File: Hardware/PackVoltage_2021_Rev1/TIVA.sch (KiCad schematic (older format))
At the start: 1 part, among them U1 TM4C129E_Launchpad

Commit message: Fixed Hierarchial Pins/Labels
Removed Hierarchal labels from top sheet and replaced them with pins linked to the subsheets.
Renamed M5 Tiva pin to D1
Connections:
- net labels added: Current_Sensor_D1, Driver_D1
- net labels removed: Current_Sensor_M5, Driver_M5
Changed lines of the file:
@@
 Wire Wire Line
 	6050 1900 6150 1900
-Text HLabel 6150 1700 2    50   Input ~ 0
-Current_Sensor_M5
-Text HLabel 6150 1900 2    50   Output ~ 0
-Driver_M5
 Wire Wire Line
 	6050 1800 6150 1800
@@
 Driver_A1
 NoConn ~ 1500 3800
+Text HLabel 6150 1900 2    50   Output ~ 0
+Driver_D1
+Text HLabel 6150 1700 2    50   Input ~ 0
+Current_Sensor_D1
 $EndSCHEMATC

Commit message: added extra 12V pin to TIVA
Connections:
- net labels added: ExtraCTL
- wire segments 43 -> 44
- no-connect marks 45 -> 44
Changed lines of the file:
@@
 NoConn ~ 1500 4000
 NoConn ~ 1500 4100
-NoConn ~ 1500 4400
 NoConn ~ 2500 4200
 Text HLabel 1350 1200 1    50   Input ~ 0
@@
 Text HLabel 6150 1700 2    50   Input ~ 0
 Current_Sensor_D1
+Text HLabel 1400 4400 0    50   Output ~ 0
+ExtraCTL
+Wire Wire Line
+	1500 4400 1400 4400
 $EndSCHEMATC

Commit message: Added GimbalSense, reannotated
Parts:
- renumbered U1 to U24
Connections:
- net labels added: GimbalSense
- wire segments 44 -> 45
- no-connect marks 44 -> 43
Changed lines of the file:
@@
 $EndDescr
 $Comp
-L MRDT_Shields:TM4C129E_Launchpad U1
+L MRDT_Shields:TM4C129E_Launchpad U24
 U 2 1 5F7739FC
 P 2300 2150
-F 0 "U1" H 2331 3427 60  0000 C CNN
+F 0 "U24" H 2331 3427 60  0000 C CNN
 F 1 "TM4C129E_Launchpad" H 2331 3321 60  0000 C CNN
 F 2 "" H 2300 2150 60  0001 C CNN
@@
 $EndComp
 $Comp
-L MRDT_Shields:TM4C129E_Launchpad U1
+L MRDT_Shields:TM4C129E_Launchpad U24
 U 1 1 5F776678
 P 1700 2150
-F 0 "U1" H 1650 2000 60  0000 L CNN
+F 0 "U24" H 1650 2000 60  0000 L CNN
 F 1 "TM4C129E_Launchpad" H 1300 1850 60  0000 L CNN
 F 2 "" H 1700 2150 60  0001 C CNN
@@
 	2750 2000 2500 2000
 $Comp
-L MRDT_Shields:TM4C129E_Launchpad U1
+L MRDT_Shields:TM4C129E_Launchpad U24
 U 3 1 5F782FEC
 P 5200 2150
-F 0 "U1" H 5100 1950 60  0000 L CNN
+F 0 "U24" H 5100 1950 60  0000 L CNN
 F 1 "TM4C129E_Launchpad" H 4700 1800 60  0000 L CNN
 F 2 "" H 5200 2150 60  0001 C CNN
@@
 $EndComp
 $Comp
-L MRDT_Shields:TM4C129E_Launchpad U1
+L MRDT_Shields:TM4C129E_Launchpad U24
 U 4 1 5F7858A1
 P 5850 2150
-F 0 "U1" H 5881 3427 60  0000 C CNN
+F 0 "U24" H 5881 3427 60  0000 C CNN
 F 1 "TM4C129E_Launchpad" H 5881 3321 60  0000 C CNN
 F 2 "" H 5850 2150 60  0001 C CNN
@@
 $EndComp
 $Comp
-L MRDT_Shields:TM4C129E_Launchpad U1
+L MRDT_Shields:TM4C129E_Launchpad U24
 U 5 1 5F78B804
 P 1700 4550
-F 0 "U1" H 1700 4450 60  0000 L CNN
+F 0 "U24" H 1700 4450 60  0000 L CNN
 F 1 "TM4C129E_Launchpad" H 1200 4300 60  0000 L CNN
 F 2 "" H 1700 4550 60  0001 C CNN
@@
 $EndComp
 $Comp
-L MRDT_Shields:TM4C129E_Launchpad U1
+L MRDT_Shields:TM4C129E_Launchpad U24
 U 6 1 5F78DDF8
 P 2300 4550
-F 0 "U1" H 2331 5827 60  0000 C CNN
+F 0 "U24" H 2331 5827 60  0000 C CNN
 F 1 "TM4C129E_Launchpad" H 2331 5721 60  0000 C CNN
 F 2 "" H 2300 4550 60  0001 C CNN
@@
 $EndComp
 $Comp
-L MRDT_Shields:TM4C129E_Launchpad U1
+L MRDT_Shields:TM4C129E_Launchpad U24
 U 7 1 5F78FF89
 P 5050 4450
-F 0 "U1" H 4950 4300 60  0000 L CNN
+F 0 "U24" H 4950 4300 60  0000 L CNN
 F 1 "TM4C129E_Launchpad" H 4550 4200 60  0000 L CNN
 F 2 "" H 5050 4450 60  0001 C CNN
@@
 $EndComp
 $Comp
-L MRDT_Shields:TM4C129E_Launchpad U1
+L MRDT_Shields:TM4C129E_Launchpad U24
 U 8 1 5F79167F
 P 5750 4450
-F 0 "U1" H 5781 5727 60  0000 C CNN
+F 0 "U24" H 5781 5727 60  0000 C CNN
 F 1 "TM4C129E_Launchpad" H 5781 5621 60  0000 C CNN
 F 2 "" H 5750 4450 60  0001 C CNN
@@
 $EndComp
 $Comp
-L power:GND #PWR015
+L power:GND #PWR063
 U 1 1 5F7A24D9
 P 2800 1150
-F 0 "#PWR015" H 2800 900 50  0001 C CNN
+F 0 "#PWR063" H 2800 900 50  0001 C CNN
 F 1 "GND" H 2805 977 50  0000 C CNN
 F 2 "" H 2800 1150 50  0001 C CNN
@@
 	2650 1150 2800 1150
 $Comp
-L power:GND #PWR048
+L power:GND #PWR064
 U 1 1 5F7A423F
 P 2800 3550
-F 0 "#PWR048" H 2800 3300 50  0001 C CNN
+F 0 "#PWR064" H 2800 3300 50  0001 C CNN
 F 1 "GND" H 2805 3377 50  0000 C CNN
 F 2 "" H 2800 3550 50  0001 C CNN
@@
 	2650 3550 2800 3550
 $Comp
-L power:GND #PWR049
+L power:GND #PWR065
 U 1 1 5F7A4B62
 P 6250 3350
-F 0 "#PWR049" H 6250 3100 50  0001 C CNN
+F 0 "#PWR065" H 6250 3100 50  0001 C CNN
 F 1 "GND" H 6255 3177 50  0000 C CNN
 F 2 "" H 6250 3350 50  0001 C CNN
@@
 	6100 3350 6250 3350
 $Comp
-L power:GND #PWR062
+L power:GND #PWR066
 U 1 1 5F7A5110
 P 6350 1050
-F 0 "#PWR062" H 6350 800 50  0001 C CNN
+F 0 "#PWR066" H 6350 800 50  0001 C CNN
 F 1 "GND" H 6355 877 50  0000 C CNN
 F 2 "" H 6350 1050 50  0001 C CNN
@@
 NoConn ~ 2500 3600
 NoConn ~ 2500 4300
-NoConn ~ 1500 3700
 NoConn ~ 1500 3900
 NoConn ~ 4850 3500
@@
 Wire Wire Line
 	1500 4400 1400 4400
+Text HLabel 1400 3700 0    50   Input ~ 0
+GimbalSense
+Wire Wire Line
+	1400 3700 1500 3700
 $EndSCHEMATC

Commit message: updated footprints
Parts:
- U24: footprint (none) -> MRDT_Shields:TM4C129E_Launchpad_FULL_SMD_TOP; symbol MRDT_Shields:TM4C129E_Launchpad -> PackVoltage_2021_Rev1-rescue:TM4C129E_Launchpad-MRDT_Shields
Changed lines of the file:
@@
 $EndDescr
 $Comp
-L MRDT_Shields:TM4C129E_Launchpad U24
+L PackVoltage_2021_Rev1-rescue:TM4C129E_Launchpad-MRDT_Shields U24
 U 2 1 5F7739FC
 P 2300 2150
 F 0 "U24" H 2331 3427 60  0000 C CNN
 F 1 "TM4C129E_Launchpad" H 2331 3321 60  0000 C CNN
-F 2 "" H 2300 2150 60  0001 C CNN
+F 2 "MRDT_Shields:TM4C129E_Launchpad_FULL_SMD_TOP" H 2300 2150 60  0001 C CNN
 F 3 "" H 2300 2150 60  0001 C CNN
 	2    2300 2150
@@
 $EndComp
 $Comp
-L MRDT_Shields:TM4C129E_Launchpad U24
+L PackVoltage_2021_Rev1-rescue:TM4C129E_Launchpad-MRDT_Shields U24
 U 1 1 5F776678
 P 1700 2150
 F 0 "U24" H 1650 2000 60  0000 L CNN
 F 1 "TM4C129E_Launchpad" H 1300 1850 60  0000 L CNN
-F 2 "" H 1700 2150 60  0001 C CNN
+F 2 "MRDT_Shields:TM4C129E_Launchpad_FULL_SMD_TOP" H 1700 2150 60  0001 C CNN
 F 3 "" H 1700 2150 60  0001 C CNN
 	1    1700 2150
@@
 	2750 2000 2500 2000
 $Comp
-L MRDT_Shields:TM4C129E_Launchpad U24
+L PackVoltage_2021_Rev1-rescue:TM4C129E_Launchpad-MRDT_Shields U24
 U 3 1 5F782FEC
 P 5200 2150
 F 0 "U24" H 5100 1950 60  0000 L CNN
 F 1 "TM4C129E_Launchpad" H 4700 1800 60  0000 L CNN
-F 2 "" H 5200 2150 60  0001 C CNN
+F 2 "MRDT_Shields:TM4C129E_Launchpad_FULL_SMD_TOP" H 5200 2150 60  0001 C CNN
 F 3 "" H 5200 2150 60  0001 C CNN
 	3    5200 2150
@@
 $EndComp
 $Comp
-L MRDT_Shields:TM4C129E_Launchpad U24
+L PackVoltage_2021_Rev1-rescue:TM4C129E_Launchpad-MRDT_Shields U24
 U 4 1 5F7858A1
 P 5850 2150
 F 0 "U24" H 5881 3427 60  0000 C CNN
 F 1 "TM4C129E_Launchpad" H 5881 3321 60  0000 C CNN
-F 2 "" H 5850 2150 60  0001 C CNN
+F 2 "MRDT_Shields:TM4C129E_Launchpad_FULL_SMD_TOP" H 5850 2150 60  0001 C CNN
 F 3 "" H 5850 2150 60  0001 C CNN
 	4    5850 2150
@@
 $EndComp
 $Comp
-L MRDT_Shields:TM4C129E_Launchpad U24
+L PackVoltage_2021_Rev1-rescue:TM4C129E_Launchpad-MRDT_Shields U24
 U 5 1 5F78B804
 P 1700 4550
 F 0 "U24" H 1700 4450 60  0000 L CNN
 F 1 "TM4C129E_Launchpad" H 1200 4300 60  0000 L CNN
-F 2 "" H 1700 4550 60  0001 C CNN
+F 2 "MRDT_Shields:TM4C129E_Launchpad_FULL_SMD_TOP" H 1700 4550 60  0001 C CNN
 F 3 "" H 1700 4550 60  0001 C CNN
 	5    1700 4550
@@
 $EndComp
 $Comp
-L MRDT_Shields:TM4C129E_Launchpad U24
+L PackVoltage_2021_Rev1-rescue:TM4C129E_Launchpad-MRDT_Shields U24
 U 6 1 5F78DDF8
 P 2300 4550
 F 0 "U24" H 2331 5827 60  0000 C CNN
 F 1 "TM4C129E_Launchpad" H 2331 5721 60  0000 C CNN
-F 2 "" H 2300 4550 60  0001 C CNN
+F 2 "MRDT_Shields:TM4C129E_Launchpad_FULL_SMD_TOP" H 2300 4550 60  0001 C CNN
 F 3 "" H 2300 4550 60  0001 C CNN
 	6    2300 4550
@@
 $EndComp
 $Comp
-L MRDT_Shields:TM4C129E_Launchpad U24
+L PackVoltage_2021_Rev1-rescue:TM4C129E_Launchpad-MRDT_Shields U24
 U 7 1 5F78FF89
 P 5050 4450
 F 0 "U24" H 4950 4300 60  0000 L CNN
 F 1 "TM4C129E_Launchpad" H 4550 4200 60  0000 L CNN
-F 2 "" H 5050 4450 60  0001 C CNN
+F 2 "MRDT_Shields:TM4C129E_Launchpad_FULL_SMD_TOP" H 5050 4450 60  0001 C CNN
 F 3 "" H 5050 4450 60  0001 C CNN
 	7    5050 4450
@@
 $EndComp
 $Comp
-L MRDT_Shields:TM4C129E_Launchpad U24
+L PackVoltage_2021_Rev1-rescue:TM4C129E_Launchpad-MRDT_Shields U24
 U 8 1 5F79167F
 P 5750 4450
 F 0 "U24" H 5781 5727 60  0000 C CNN
 F 1 "TM4C129E_Launchpad" H 5781 5621 60  0000 C CNN
-F 2 "" H 5750 4450 60  0001 C CNN
+F 2 "MRDT_Shields:TM4C129E_Launchpad_FULL_SMD_TOP" H 5750 4450 60  0001 C CNN
 F 3 "" H 5750 4450 60  0001 C CNN
 	8    5750 4450

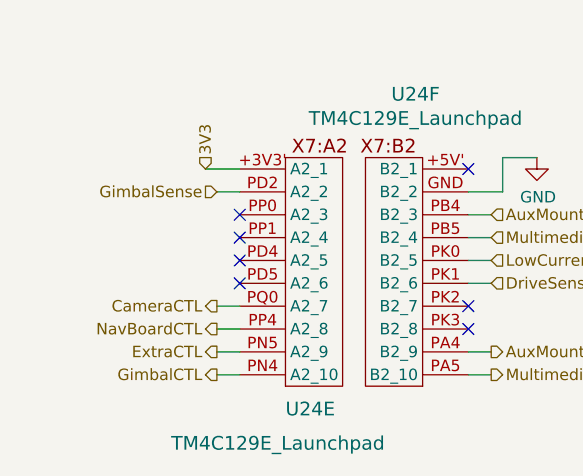
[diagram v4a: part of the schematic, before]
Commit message: added DriveCTL to MOLEX and TIVA, changed andersons to actuation
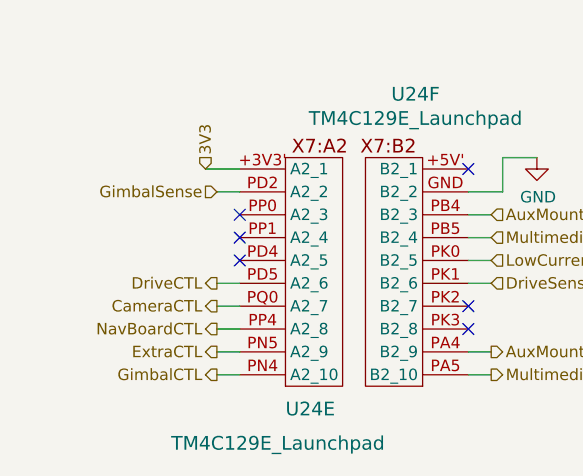
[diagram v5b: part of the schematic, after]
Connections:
- net DriveCTL: now reaches U24.PD5 (A2_6)
- no-connect marks 43 -> 42
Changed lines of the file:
@@
 Driver_T1
 NoConn ~ 1500 4000
-NoConn ~ 1500 4100
 NoConn ~ 2500 4200
 Text HLabel 1350 1200 1    50   Input ~ 0
@@
 Wire Wire Line
 	1400 3700 1500 3700
+Text HLabel 1400 4100 0    50   Output ~ 0
+DriveCTL
+Wire Wire Line
+	1400 4100 1500 4100
 $EndSCHEMATC

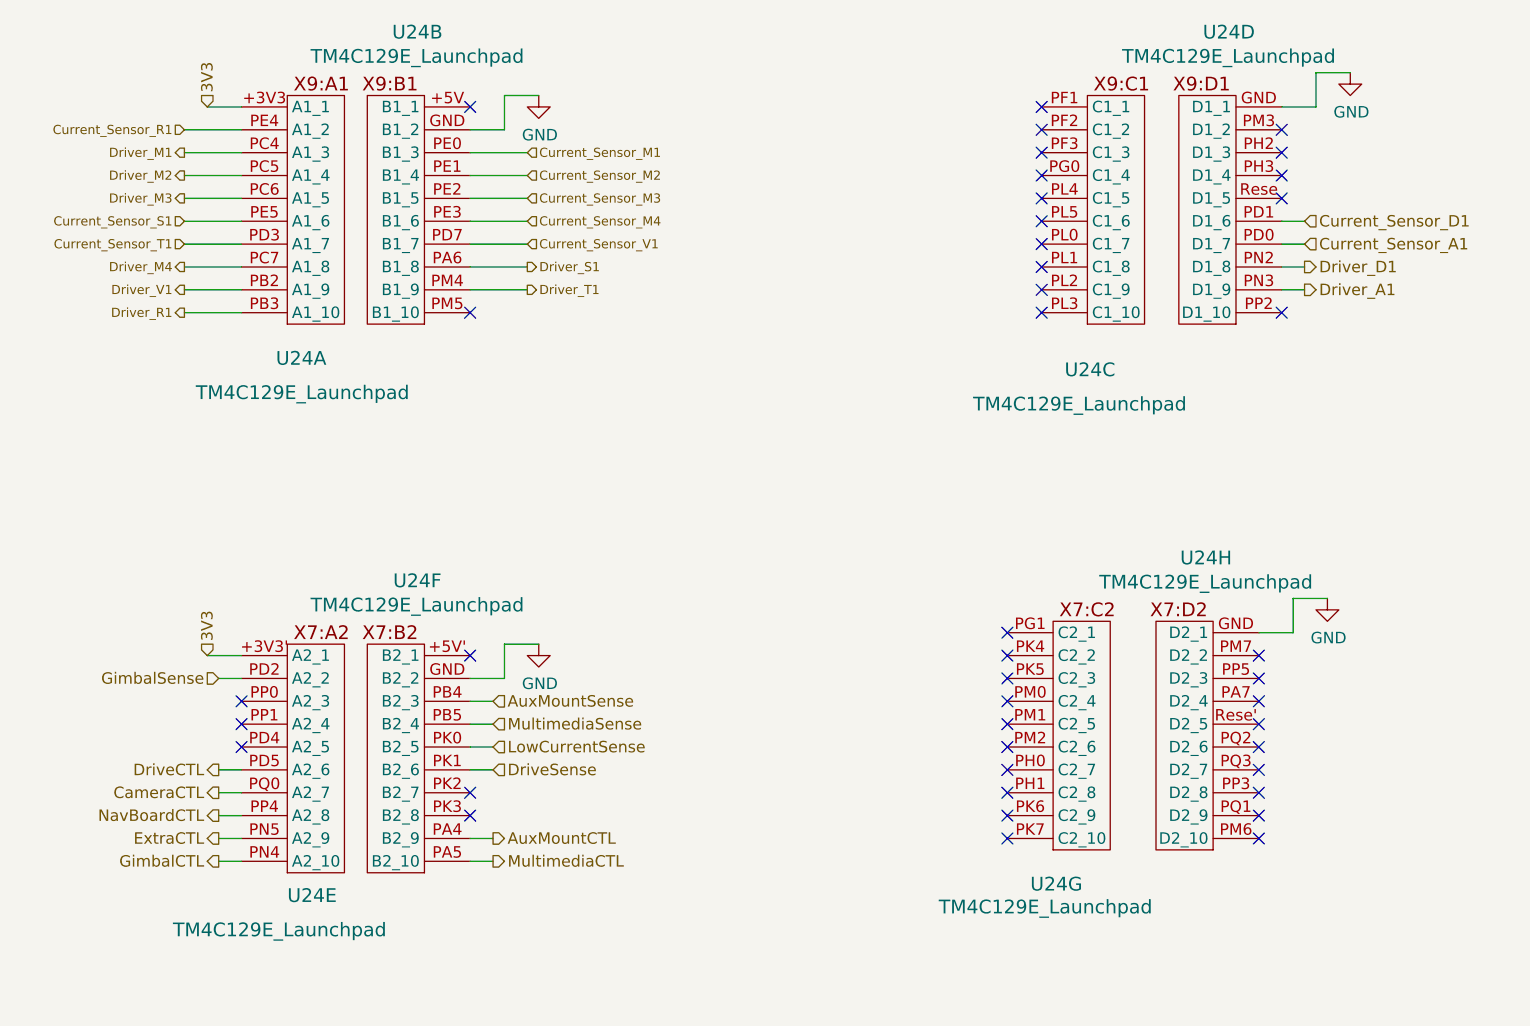
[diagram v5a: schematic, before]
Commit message: Changed 12V Connectors
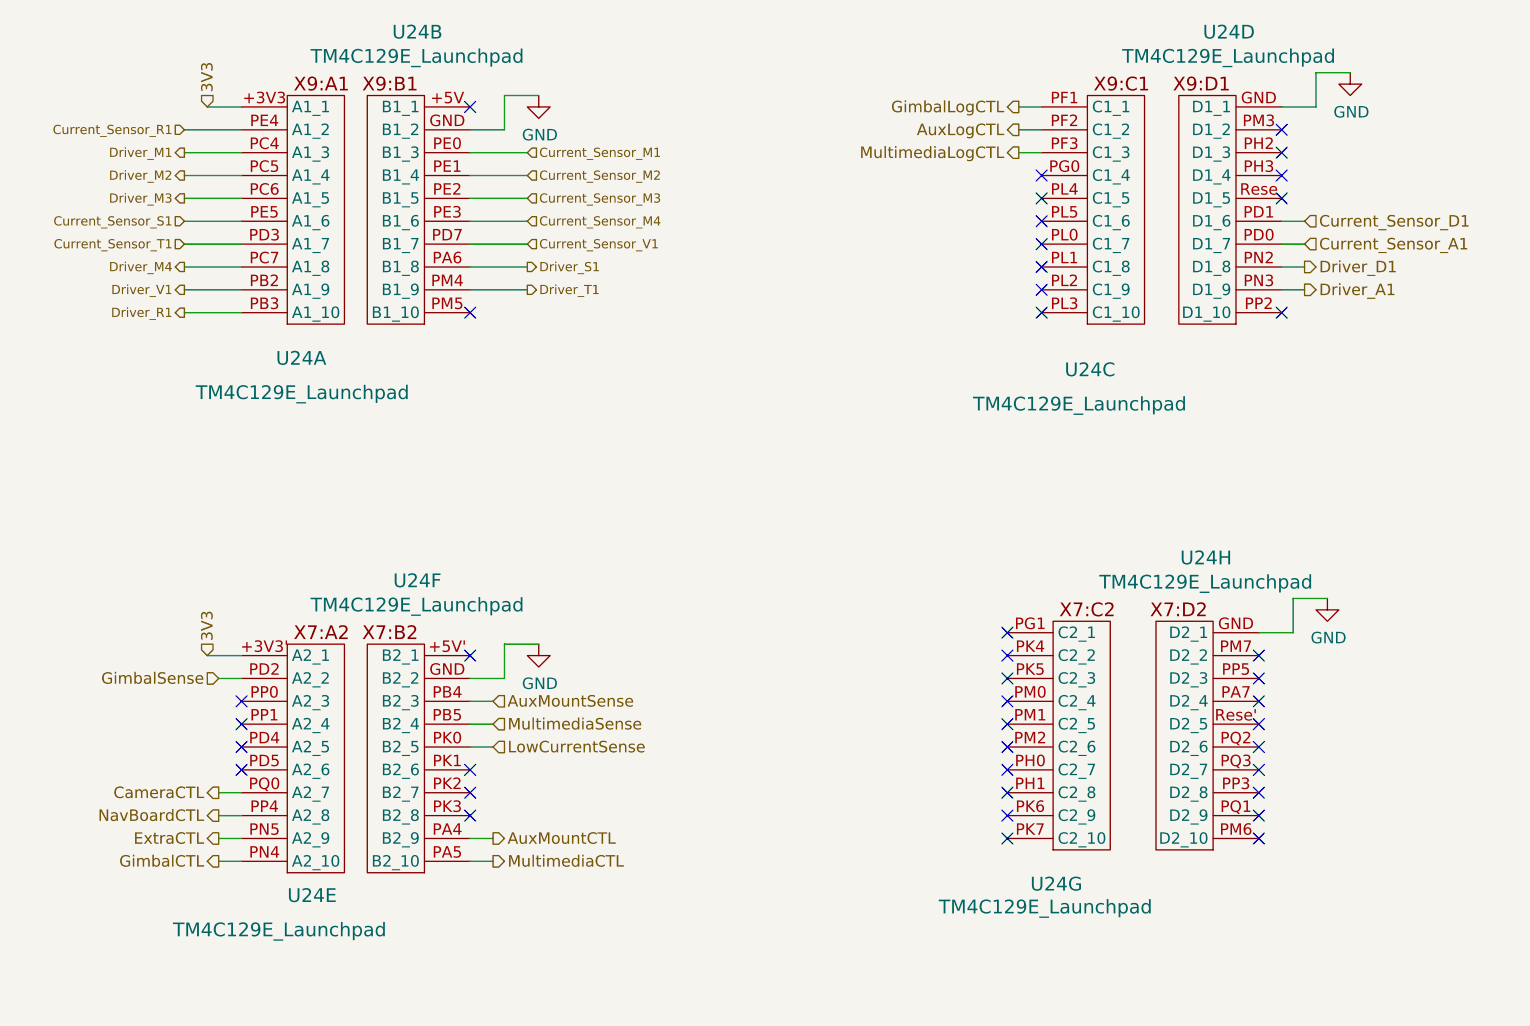
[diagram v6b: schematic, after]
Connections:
- net GimbalLogCTL: now reaches U24.PF1 (C1_1)
- net AuxLogCTL: now reaches U24.PF2 (C1_2)
- net MultimediaLogCTL: now reaches U24.PF3 (C1_3)
- net DriveCTL: no longer names the net of U24.PD5 (A2_6)
- net DriveSense: no longer names the net of U24.PK1 (B2_6)
- no-connect marks 42 -> 41
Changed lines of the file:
@@
 Wire Wire Line
 	6200 1050 6350 1050
-NoConn ~ 5000 1200
-NoConn ~ 5000 1300
-NoConn ~ 5000 1400
 NoConn ~ 5000 1500
 NoConn ~ 5000 1600
@@
 Wire Wire Line
 	2500 4000 2600 4000
-Wire Wire Line
-	2500 4100 2600 4100
 Wire Wire Line
 	2500 4400 2600 4400
@@
 Text HLabel 2600 4000 2    50   Input ~ 0
 LowCurrentSense
-Text HLabel 2600 4100 2    50   Input ~ 0
-DriveSense
 Text HLabel 2600 4400 2    50   Output ~ 0
 AuxMountCTL
@@
 Wire Wire Line
 	1400 3700 1500 3700
-Text HLabel 1400 4100 0    50   Output ~ 0
-DriveCTL
+NoConn ~ 2500 4100
 Wire Wire Line
-	1400 4100 1500 4100
+	5000 1200 4900 1200
+Wire Wire Line
+	5000 1300 4900 1300
+Wire Wire Line
+	5000 1400 4900 1400
+Text HLabel 4900 1200 0    50   Output ~ 0
+GimbalLogCTL
+Text HLabel 4900 1300 0    50   Output ~ 0
+AuxLogCTL
+Text HLabel 4900 1400 0    50   Output ~ 0
+MultimediaLogCTL
+NoConn ~ 1500 4100
 $EndSCHEMATC

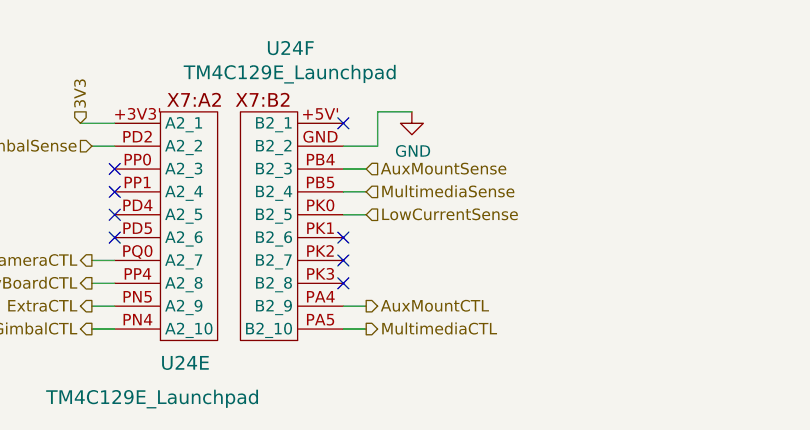
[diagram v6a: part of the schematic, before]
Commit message: added all components to board
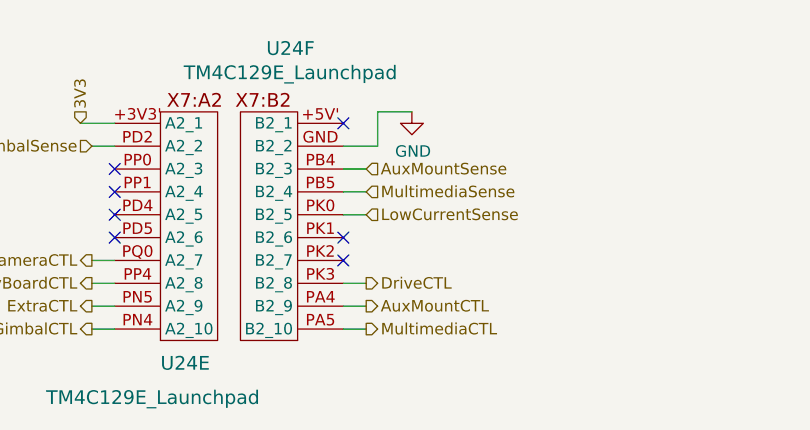
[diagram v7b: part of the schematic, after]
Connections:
- net DriveCTL: now reaches U24.PK3 (B2_8)
- no-connect marks 41 -> 40
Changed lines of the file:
@@
 	2500 4500 2600 4500
 NoConn ~ 2500 3600
-NoConn ~ 2500 4300
 NoConn ~ 1500 3900
 NoConn ~ 4850 3500
@@
 MultimediaLogCTL
 NoConn ~ 1500 4100
+Text HLabel 2600 4300 2    50   Output ~ 0
+DriveCTL
+Wire Wire Line
+	2600 4300 2500 4300
 $EndSCHEMATC
